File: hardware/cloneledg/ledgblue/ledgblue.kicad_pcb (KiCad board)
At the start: 2 copper layers, 71.4 x 54.2 mm, 60 parts, among them J1 USB_OTG, P1 DEBUG, P2 DEBUG, P3 YL035MY2, P4 YL035MY2_TS_WURTH, SW1 WURTH 436353045816, SW2 SW-PB, U1 LD39020_3.0V, U2 STMPS2151TTR, U3 ST31G480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

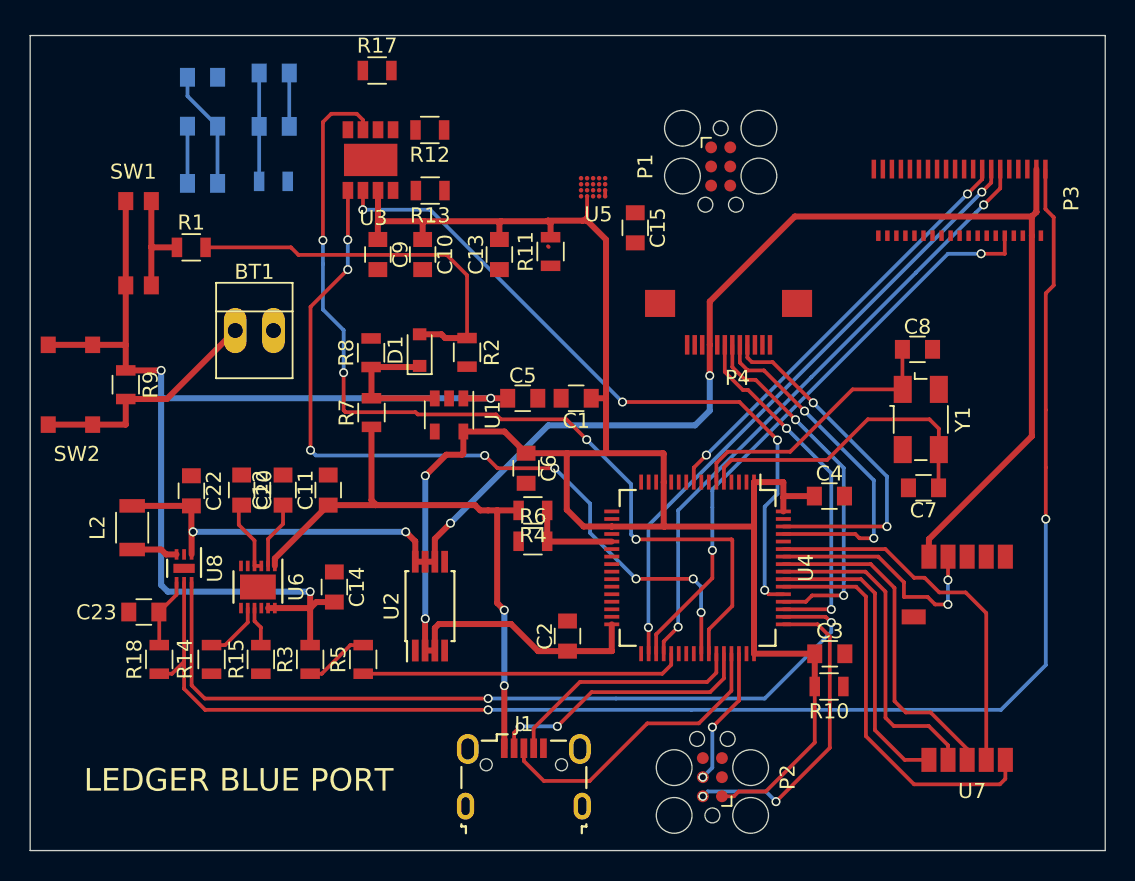
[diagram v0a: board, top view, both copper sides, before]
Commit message: Layout has been compacted
The layout has been shrunk a bit. A pin header is used as placeholder for the antenna. NFC chip still not connected.
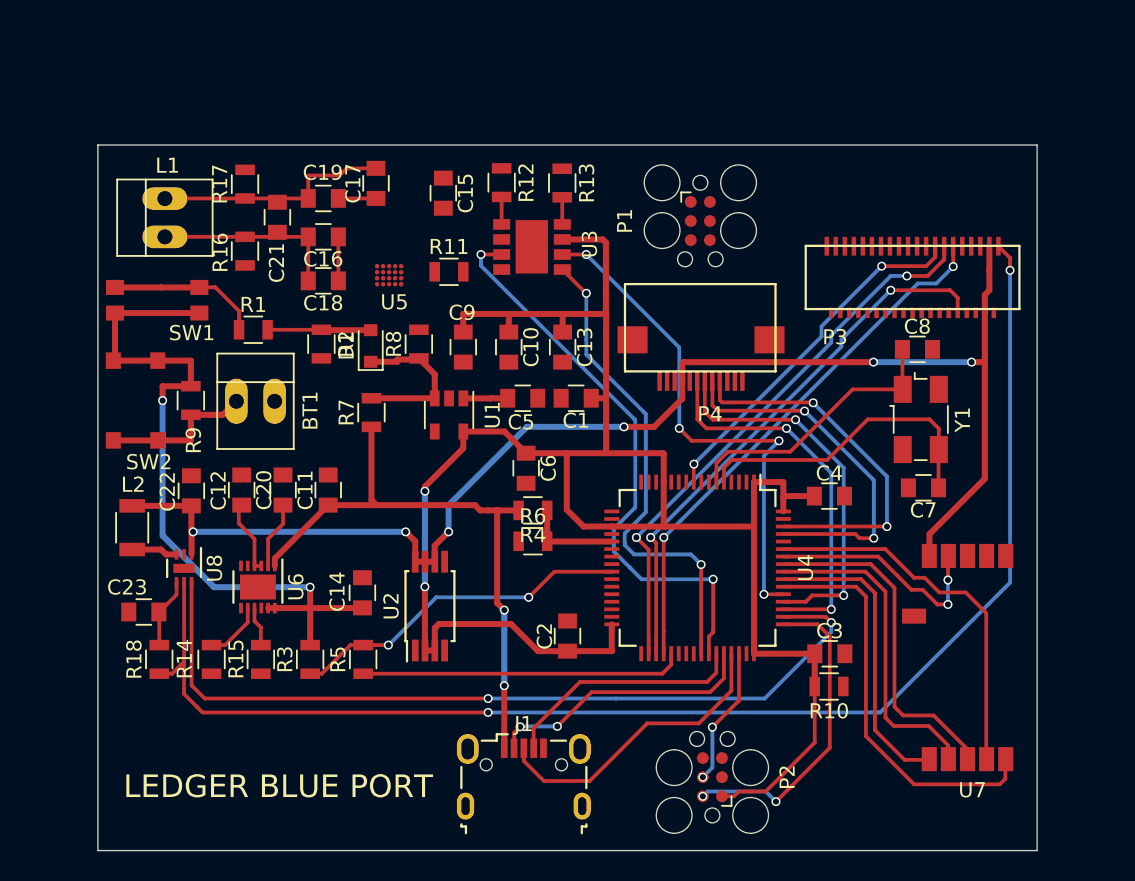
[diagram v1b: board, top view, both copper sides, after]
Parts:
- added L1: Antenna, Connectors:PINHEAD1-2, F.Cu at (30.2, 143.7)
- C16, C17, C18, C19, C21, R16: moved to F.Cu
- moved U3 16.9 mm to (57.5, 146.8), turned to 90 degrees
- moved U5 14.8 mm to (44.4, 146.8)
- moved C18 14.2 mm to (40.8, 146.6)
- moved C15 13.0 mm to (48.8, 140.8)
- moved C17 12.1 mm to (44.3, 140.2), turned to 90 degrees
- moved R17 11.6 mm to (35.6, 140.2), turned to 90 degrees
- moved C21 10.5 mm to (37.7, 142.4), turned to 90 degrees
- moved R2 9.69 mm to (40.6, 150.8)
- moved R13 8.79 mm to (56.6, 140.1), turned to 270 degrees
- moved C10 8.40 mm to (53.1, 151.0)
- moved C9 8.37 mm to (50.1, 151.0)
- moved C19 8.09 mm to (40.8, 141.2), turned to 180 degrees
- moved C16 8.03 mm to (40.8, 143.7)
- moved C13 7.45 mm to (56.7, 151.0)
- moved R11 6.88 mm to (49.1, 146.0), turned to 0 degrees
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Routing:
- net SE_IO: track 63.0 -> 38.4 mm, vias 4 -> 2
- net +BATT: track 76.1 -> 51.8 mm, vias 3 -> 2
- net SE_CLK: track 53.6 -> 32.7 mm, vias 8 -> 2
- net ButtonIT: track 25.6 -> 6.86 mm
- net BC_ADC_IN: track 4.31 -> 22.8 mm, vias 0 -> 2
- net AUX_PWR: track 108.0 -> 92.2 mm, vias 4 -> 6
- net SE_RST: track 46.9 -> 34.6 mm
- net LED_A: track 101.5 -> 91.1 mm
- net MAIN_POWER: track 142.8 -> 133.7 mm
- net Net-(C17-Pad2): track 7.88 -> 15.8 mm
- net Net-(BT1-Pad1): track 16.0 -> 10.2 mm
- net Disp_SDA: track 41.5 -> 35.8 mm
- net Net-(C16-Pad2): track 7.20 -> 12.5 mm
- net Disp_RESET: track 28.7 -> 24.0 mm
- net DISP_SCL: track 41.6 -> 37.3 mm
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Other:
- board size 71.4 x 54.2 mm -> 62.4 x 46.9 mm

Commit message: Ledger Blue port finished
Everything is connected!
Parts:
- moved L2 19.6 mm to (39.0, 179.3), turned to 180 degrees
- moved R18 18.2 mm to (46.5, 179.3), turned to 270 degrees
- moved C23 18.2 mm to (43.4, 179.5), turned to 270 degrees
- moved C22 15.7 mm to (36.6, 175.6)
- moved U8 14.3 mm to (41.4, 176.1), turned to 0 degrees
- moved R13 6.30 mm to (50.4, 140.2), turned to 90 degrees
- moved C8 5.81 mm to (74.8, 153.3), turned to 90 degrees
- moved C11 5.11 mm to (40.3, 165.6), turned to 0 degrees
- moved R12 4.67 mm to (48.0, 140.2), turned to 90 degrees
- moved C15 4.63 mm to (45.1, 143.7), turned to 0 degrees
- moved C3 3.87 mm to (71.0, 173.2), turned to 180 degrees
- moved R10 3.63 mm to (71.0, 175.0), turned to 0 degrees
- moved BT1 3.59 mm to (38.1, 156.4)
- moved R9 3.54 mm to (34.1, 157.4)
- moved SW1 3.54 mm to (28.5, 149.4)
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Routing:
- net NRST: track 0.00 -> 137.4 mm, vias 0 -> 9
- net Net-(P1-Pad2): track 0.00 -> 35.6 mm, vias 0 -> 4
- net Net-(P1-Pad4): track 0.00 -> 27.5 mm, vias 0 -> 2
- net Net-(P1-Pad5): track 0.00 -> 24.6 mm, vias 0 -> 3
- net Backlight_PWM: track 55.5 -> 31.7 mm
- net LED_A: track 91.1 -> 72.4 mm
- net AUX_PWR_enable: track 0.00 -> 18.5 mm, vias 0 -> 2
- net MAIN_POWER: track 133.7 -> 148.1 mm
- net +BATT: track 51.8 -> 65.7 mm, vias 2 -> 4
- net Net-(R17-Pad2): track 0.00 -> 11.9 mm, vias 0 -> 2
- net Net-(R16-Pad2): track 0.00 -> 9.41 mm, vias 0 -> 2
- net Net-(R13-Pad1): track 0.00 -> 9.32 mm, vias 0 -> 2
- net Net-(R13-Pad2): track 1.80 -> 8.39 mm
- net Net-(R12-Pad1): track 0.00 -> 6.45 mm
- net Net-(C17-Pad1): track 2.50 -> 7.93 mm, vias 0 -> 2
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- added copper zone on B.Cu, net NRST
- added copper zone on F.Cu, net NRST
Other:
- board size 62.4 x 46.9 mm -> 60.5 x 45.8 mm
- net class Default: clearance 0.1 -> 0.05
- net class MiniVia added: clearance 0.05, trace_width 0.2, via_dia 0.3, via_drill 0.15
- rule trace_clearance: 0.1 -> 0.05
- rule via_min_drill: 0.3 -> 0.1
- rule via_min_size: 0.4 -> 0.3
